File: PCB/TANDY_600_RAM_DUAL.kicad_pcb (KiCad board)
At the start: 2 copper layers, 57.2 x 19.1 mm, 8 parts, among them CN1 TANDY_600_RAM_BUS_plain_pins, CN2 TANDY_600_RAM_BUS_plain_pins, U1 AS6C2008A, U2 HC148, U3 1G02

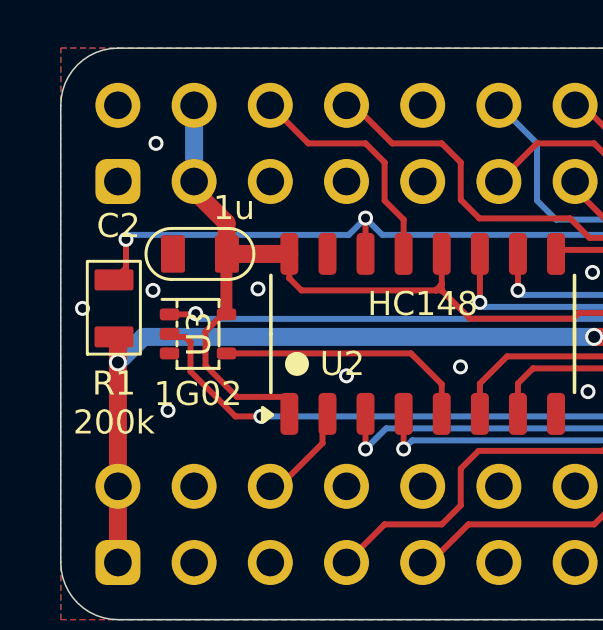
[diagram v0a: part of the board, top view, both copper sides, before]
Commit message: rename 3d dir to 3dshapes to standardize
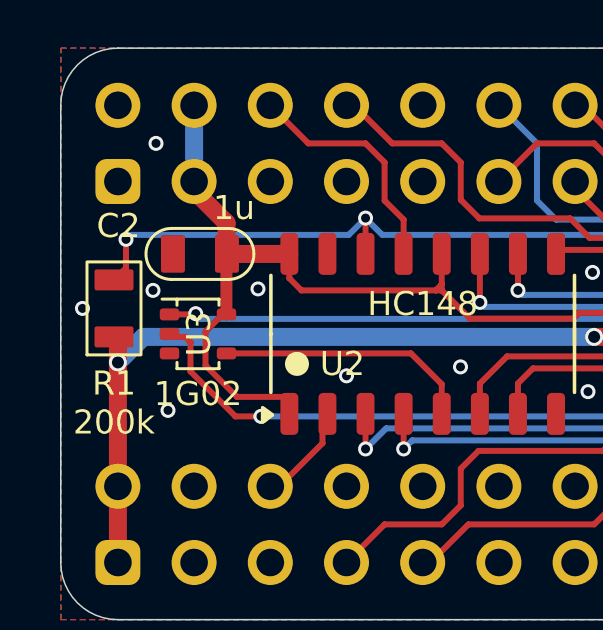
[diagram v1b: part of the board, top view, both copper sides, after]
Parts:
- U2: footprint 000_LOCAL:SOIC-16_4x10 -> 000_LOCAL:SOIC-16_3.9x9.9mm_P1.27mm

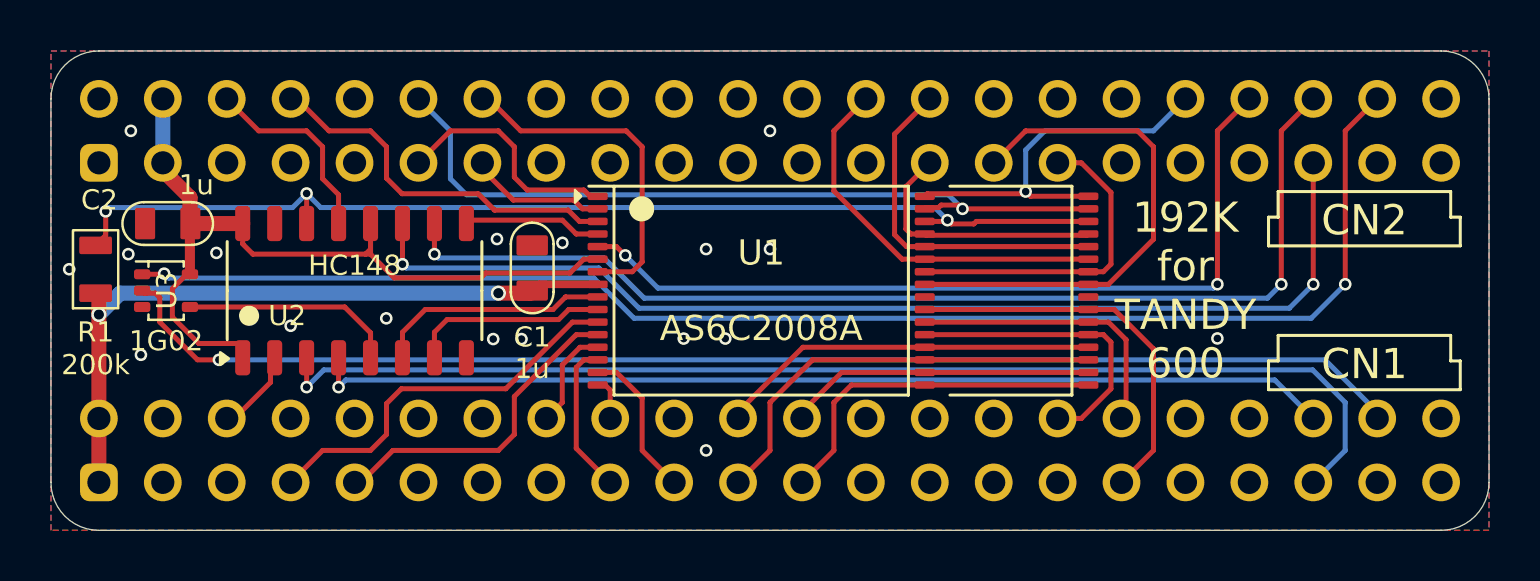
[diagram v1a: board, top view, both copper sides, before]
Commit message: dual: sch add MPNs & bom, pcb move A14,16,17
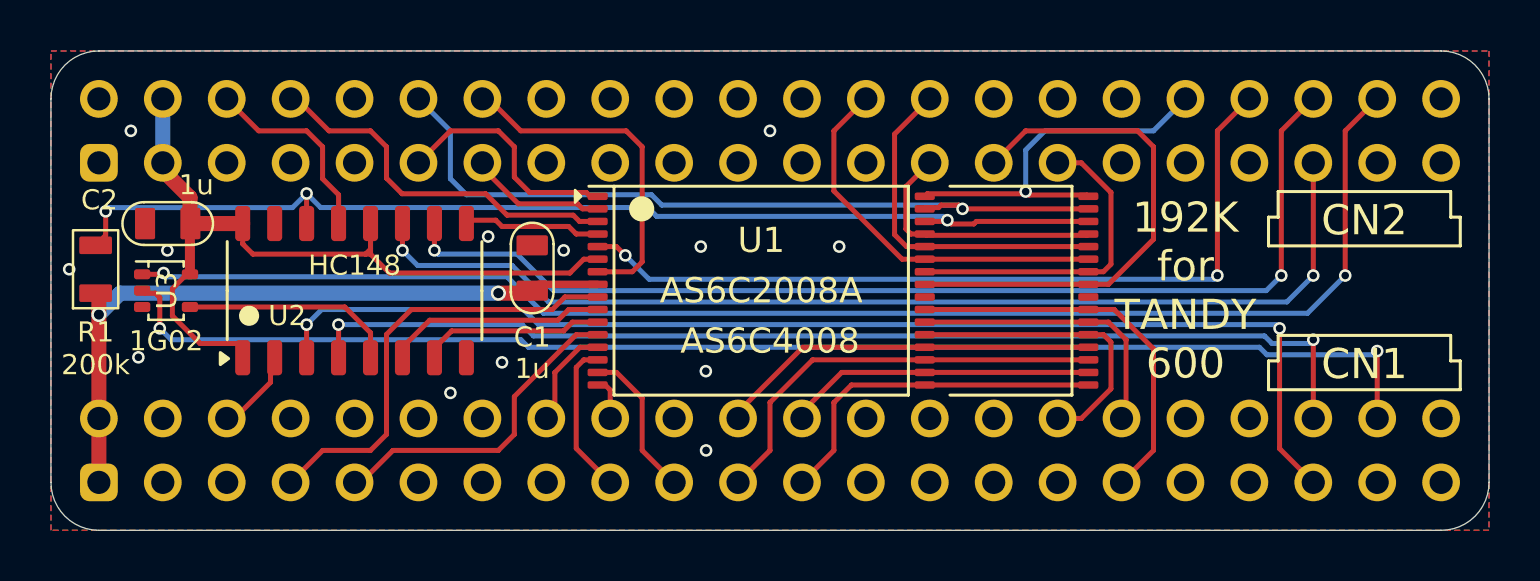
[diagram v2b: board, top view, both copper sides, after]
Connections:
- U1 pad 10: /A16 -> /A17
- U1 pad 11: /A14 -> /A16
- U1 pad 9: /A17 -> /A14
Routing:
- net /~{B1_CS1_B}: track 40.7 -> 43.6 mm, vias 1 -> 2
- net /A14: track 15.6 -> 17.6 mm
- net /B1_CS2: track 51.9 -> 53.6 mm, vias 1 -> 2
- net /~{B2_CS1_C}: track 43.8 -> 43.0 mm
- net /A16: track 7.87 -> 7.30 mm
- net /A17: track 9.35 -> 8.79 mm
- net /~{B2_CS1_B}: track 43.7 -> 43.2 mm
- net /~{B1_CS1_C}: track 47.0 -> 47.2 mm, vias 1 -> 2
- net GND: vias 18 -> 13
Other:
- board text added: "AS6C4008"

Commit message: dual: relocate chips for shorter traces & fewer vias, add service manual
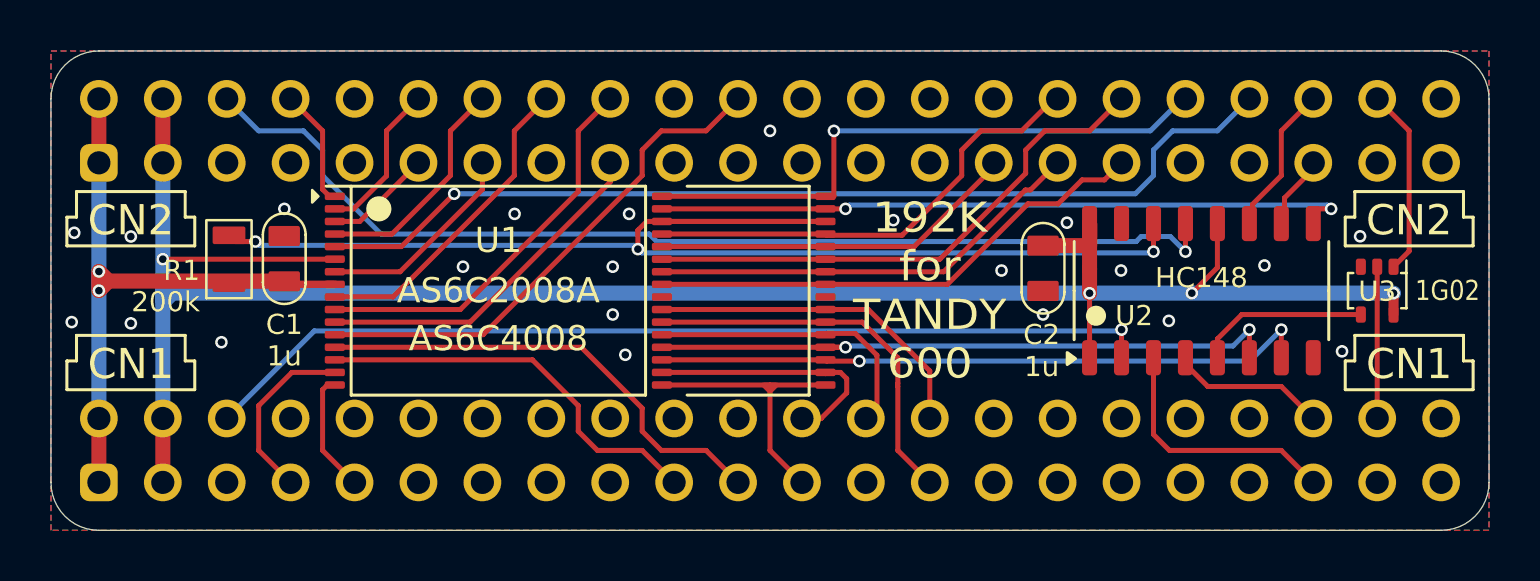
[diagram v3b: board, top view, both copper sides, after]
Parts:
- moved U3 48.1 mm to (175.3, 109.2), turned to -90 degrees
- moved C2 34.8 mm to (162.0, 108.3), turned to -90 degrees
- moved U2 33.7 mm to (168.3, 109.2)
- moved U1 10.4 mm to (140.3, 109.2)
- moved C1 9.86 mm to (131.8, 108.0)
- moved R1 5.32 mm to (129.6, 108.0)
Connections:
- CN1 pad a14: unconnected-(CN1-D6-Pada14) -> /D6
- CN1 pad a17: /D1 -> unconnected-(CN1-D1-Pada17)
- CN1 pad a2: unconnected-(CN1-VCC-Pada2) -> VCC
- CN1 pad a9: /A6 -> unconnected-(CN1-A6-Pada9)
- CN1 pad b11: /A2 -> unconnected-(CN1-A2-Padb11)
- CN1 pad b13: unconnected-(CN1-D7-Padb13) -> /D7
- CN1 pad b14: unconnected-(CN1-D5-Padb14) -> /D5
- CN1 pad b15: unconnected-(CN1-NC-Padb15) -> GND
- CN1 pad b16: /D2 -> unconnected-(CN1-D2-Padb16)
- CN1 pad b17: /D0 -> unconnected-(CN1-D0-Padb17)
- CN1 pad b2: unconnected-(CN1-VCC-Padb2) -> VCC
- CN1 pad b8: /A7 -> unconnected-(CN1-A7-Padb8)
- CN1 pad b9: /A5 -> unconnected-(CN1-A5-Padb9)
- CN2 pad a1: unconnected-(CN2-VMEM-Pada1) -> VMEM
- CN2 pad a14: /D6 -> unconnected-(CN2-D6-Pada14)
- CN2 pad a17: unconnected-(CN2-D1-Pada17) -> /D1
- CN2 pad a9: unconnected-(CN2-A6-Pada9) -> /A6
- CN2 pad b1: unconnected-(CN2-VMEM-Padb1) -> VMEM
- CN2 pad b11: unconnected-(CN2-A2-Padb11) -> /A2
- CN2 pad b13: /D7 -> unconnected-(CN2-D7-Padb13)
- CN2 pad b14: /D5 -> unconnected-(CN2-D5-Padb14)
- CN2 pad b15: unconnected-(CN2-NC-Padb15) -> GND
- CN2 pad b16: unconnected-(CN2-D2-Padb16) -> /D2
- CN2 pad b17: unconnected-(CN2-D0-Padb17) -> /D0
- CN2 pad b8: unconnected-(CN2-A7-Padb8) -> /A7
- CN2 pad b9: unconnected-(CN2-A5-Padb9) -> /A5
- U1 pad 1: /A11 -> /A13
- U1 pad 10: /A17 -> /A5
- U1 pad 11: /A16 -> /A6
- U1 pad 12: /A12 -> /A2
- U1 pad 13: /A7 -> /A3
- U1 pad 14: /A6 -> /A4
- U1 pad 15: /A4 -> /A14
- U1 pad 16: /A5 -> /A12
- U1 pad 19: /A3 -> /A16
- U1 pad 2: /A9 -> /A10
- U1 pad 20: /A2 -> /A17
- U1 pad 21: /D2 -> /D7
- U1 pad 22: /D0 -> /D6
- U1 pad 23: /D1 -> /D5
- U1 pad 25: /D4 -> /D1
- U1 pad 27: /D7 -> /D0
- U1 pad 28: /D5 -> /D4
- U1 pad 29: /D6 -> /D2
- U1 pad 3: /A13 -> /A11
- U1 pad 31: /A10 -> /A15
- U1 pad 4: /A15 -> /A8
- U1 pad 7: /A8 -> /A9
- U1 pad 9: /A14 -> /A7
- U2 pad 10: /~{B2_CS1_B} -> /~{B2_CS1_C}
- U2 pad 11: /~{B2_CS1_C} -> /~{B2_CS1_B}
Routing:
- net VCC: track 32.5 -> 83.1 mm, vias 0 -> 4
- net /B2_CS2: track 56.7 -> 7.45 mm, vias 2 -> 0
- net /B1_CS2: track 53.6 -> 6.03 mm, vias 2 -> 0
- net /~{B2_CS1_C}: track 43.0 -> 2.94 mm, vias 2 -> 0
- net /~{B1_CS1_B}: track 43.6 -> 6.23 mm, vias 2 -> 0
- net /~{B2_CS1_B}: track 43.2 -> 6.01 mm, vias 2 -> 0
- net /~{B1_CS1_C}: track 47.2 -> 10.2 mm, vias 2 -> 0
- net /~{B1_CS1_A}: track 3.38 -> 38.1 mm, vias 0 -> 1
- net /~{B2_CS1_A}: track 7.91 -> 42.5 mm, vias 0 -> 1
- net /A10: track 31.2 -> 6.19 mm, vias 1 -> 0
- net /A15: track 5.58 -> 28.0 mm, vias 0 -> 2
- net /A16: track 7.30 -> 26.3 mm, vias 0 -> 2
- net /A17: track 8.79 -> 25.5 mm, vias 0 -> 2
- net /A5: track 1.71 -> 15.8 mm
- net /A14: track 17.6 -> 7.15 mm
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
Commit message: datasheets OPRM pinout
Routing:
- net GND: vias 22 -> 27
